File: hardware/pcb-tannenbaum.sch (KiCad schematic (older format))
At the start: 32 parts, among them J1 Conn_02x03_Counter_Clockwise, SW1 SW_Push, SW2 SW_Push, U1 TMP101, U2 ATtiny85V-10SU, U3 TPS27081A_ForReversePolarityP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

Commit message: Finish first iteration of PCB layout
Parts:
- removed C12, C4: C, Capacitor_SMD:C_0805_2012Metric_Pad1.15x1.40mm_HandSolder, symbol Device:C
- U2: symbol MCU_Microchip_ATtiny:ATtiny85V-10SU -> pcb-tannenbaum-rescue:ATtiny85V-10SU-MCU_Microchip_ATtiny
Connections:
- wire segments 90 -> 150
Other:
- moved on the sheet: C1, C11, C2, C3, C5, C6, C7, C9, D1, D10, D11, D12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

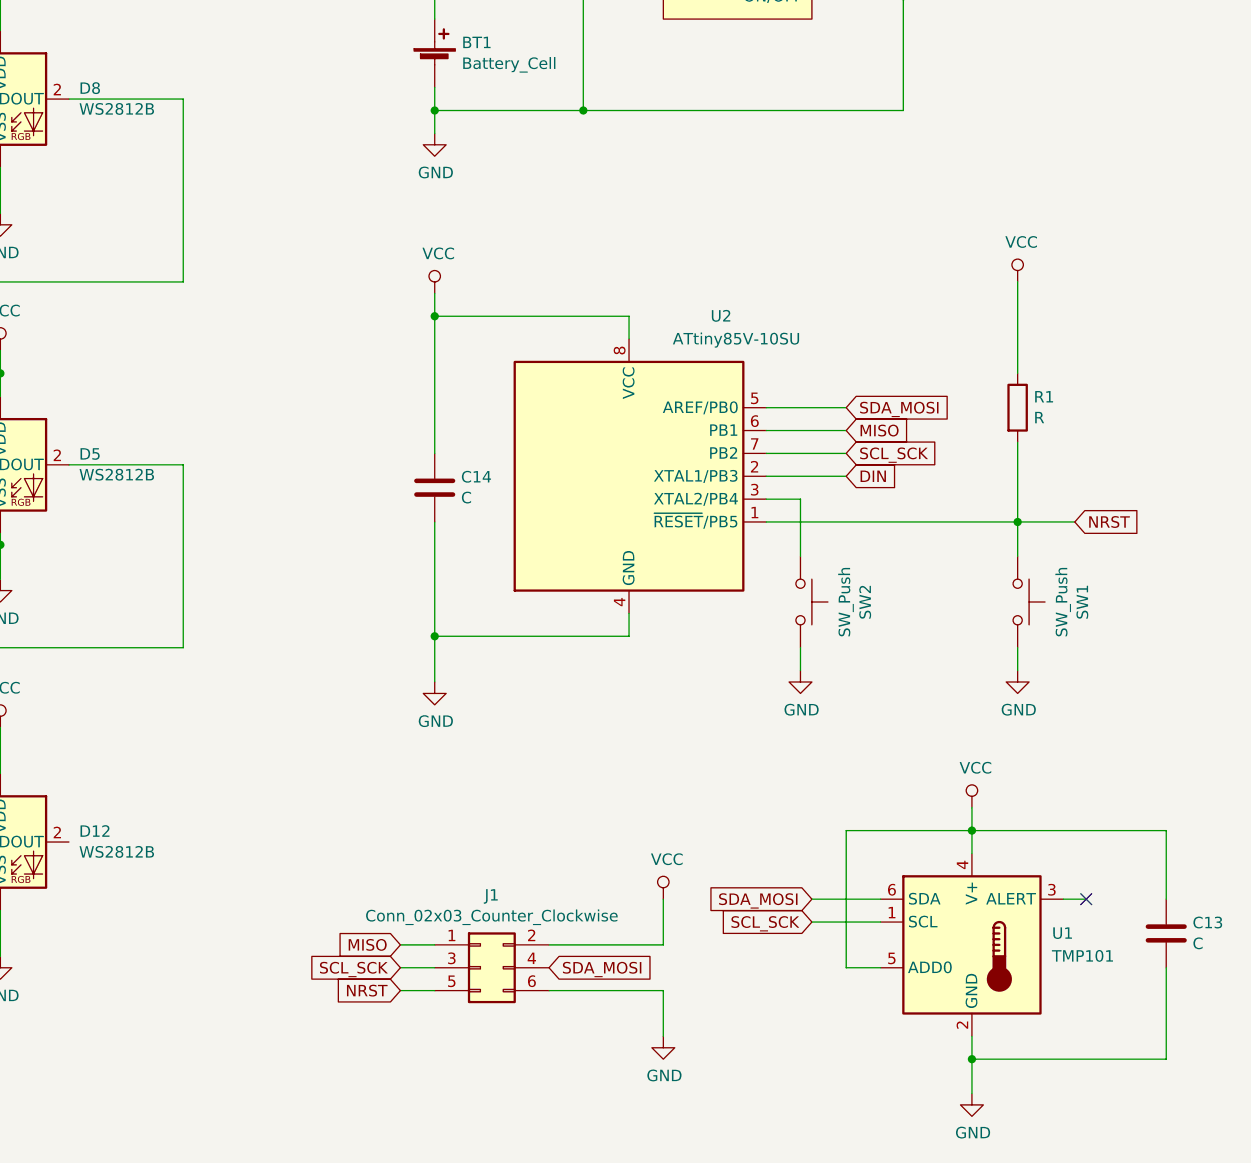
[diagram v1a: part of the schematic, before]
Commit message: Switch to STM MCU
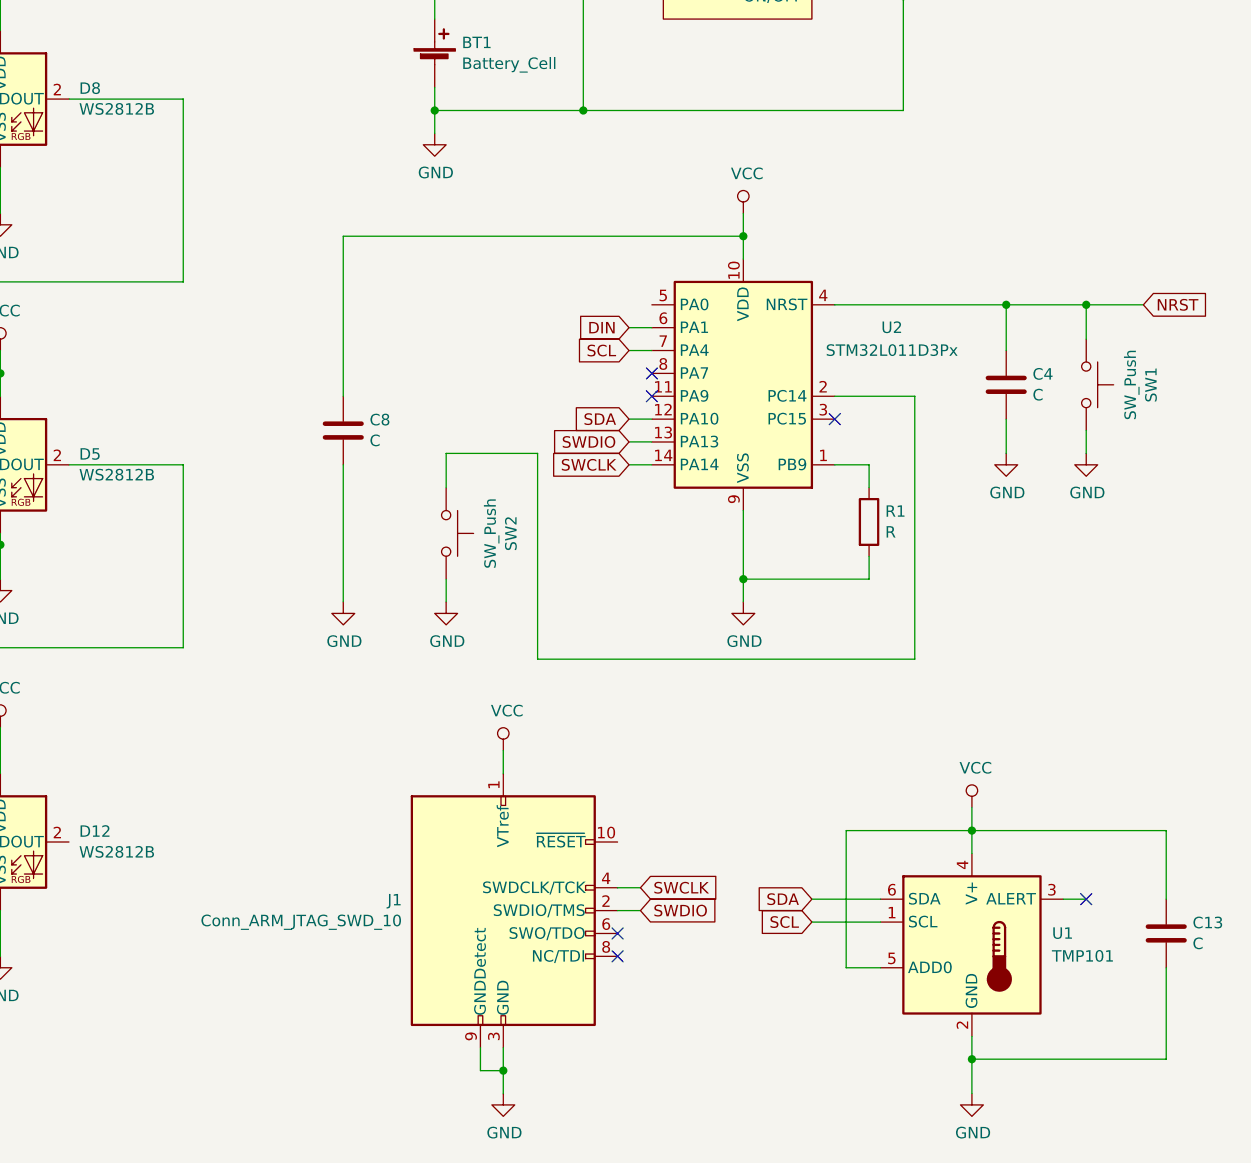
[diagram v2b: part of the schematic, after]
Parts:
- removed C14: C, Capacitor_SMD:C_0805_2012Metric_Pad1.15x1.40mm_HandSolder, symbol Device:C
- removed J1: Conn_02x03_Counter_Clockwise, Connector_PinHeader_2.54mm:PinHeader_2x03_P2.54mm_Vertical_SMD, symbol Connector_Generic:Conn_02x03_Odd_Even
- removed U2: ATtiny85V-10SU, Package_SO:SOIJ-8_5.3x5.3mm_P1.27mm, symbol pcb-tannenbaum-rescue:ATtiny85V-10SU-MCU_Microchip_ATtiny
- added C4, C8: C, Capacitor_SMD:C_0805_2012Metric_Pad1.15x1.40mm_HandSolder, symbol Device:C
- added J1: Conn_ARM_JTAG_SWD_10, Connector_PinHeader_1.27mm:PinHeader_2x05_P1.27mm_Vertical_SMD, symbol Connector:Conn_ARM_JTAG_SWD_10
- added U2: STM32L011D3Px, Package_SO:TSSOP-14_4.4x5mm_P0.65mm, symbol MCU_ST_STM32L0:STM32L011D3Px
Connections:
- net DIN: now also U2.6 (PA1)
- net GND: now also R1.2, C4.2, C8.2, J1.3 (GND), J1.5 (GND), J1.9 (GNDDetect), U2.9 (VSS)
- net NRST: now also C4.1, U2.4 (NRST); no longer R1.2
- net VCC: now also C8.1, J1.1 (VTref), U2.10 (VDD); no longer R1.1
- net at SW2.1: now also U2.2 (PC14)
- net SCL_SCK renamed SCL
- net SCL: now also U2.7 (PA4)
- net SDA_MOSI renamed SDA
- net SDA: now also U2.12 (PA10)
- new net: R1.1, U2.1 (PB9)
- new net SWCLK: J1.4 (SWDCLK/TCK), U2.14 (PA14)
- new net SWDIO: J1.2 (SWDIO/TMS), U2.13 (PA13)
- no-connect marks 1 -> 6
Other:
- moved on the sheet: SW1, SW2

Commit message: Add cube project, change buttons
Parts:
- SW1, SW2: footprint Button_Switch_SMD:SW_SPST_B3U-1000P -> Button_Switch_SMD:SW_Push_SPST_NO_Alps_SKRK
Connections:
- net NRST: now also J1.10 (~RESET~)
- no-connect marks 6 -> 9
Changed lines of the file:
@@
 F 0 "SW2" H 7650 4035 50  0000 C CNN
 F 1 "SW_Push" H 7650 3944 50  0000 C CNN
-F 2 "Button_Switch_SMD:SW_SPST_B3U-1000P" H 7650 3950 50  0001 C CNN
+F 2 "Button_Switch_SMD:SW_Push_SPST_NO_Alps_SKRK" H 7650 3950 50  0001 C CNN
 F 3 "~" H 7650 3950 50  0001 C CNN
 	1    7650 3750
@@
 F 0 "SW1" H 10450 3385 50  0000 C CNN
 F 1 "SW_Push" H 10450 3294 50  0000 C CNN
-F 2 "Button_Switch_SMD:SW_SPST_B3U-1000P" H 10450 3300 50  0001 C CNN
+F 2 "Button_Switch_SMD:SW_Push_SPST_NO_Alps_SKRK" H 10450 3300 50  0001 C CNN
 F 3 "~" H 10450 3300 50  0001 C CNN
 	1    10450 3100
 	0    1    1    0
 $EndComp
+$Comp
+L power:PWR_FLAG #FLG0102
+U 1 1 5FC68310
+P 7600 850
+F 0 "#FLG0102" H 7600 925 50  0001 C CNN
+F 1 "PWR_FLAG" H 7600 1023 50  0000 C CNN
+F 2 "" H 7600 850 50  0001 C CNN
+F 3 "~" H 7600 850 50  0001 C CNN
+	1    7600 850
+	1    0    0    -1
+$EndComp
+Wire Wire Line
+	7600 850  7600 1100
+Connection ~ 7600 1100
+NoConn ~ 6000 5100
+Text GLabel 8500 5100 2    50   Input ~ 0
+NRST
+Wire Wire Line
+	8500 5100 8400 5100
+NoConn ~ 8550 2750
+NoConn ~ 6550 1350
 $EndSCHEMATC
